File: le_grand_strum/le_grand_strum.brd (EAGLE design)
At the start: 186.9 x 99.1 mm, 101 parts, among them IC1 REG1117, IC2 PIC16F1825SO14, IC3 74HC595D, IC4 74HC595D, SW1 12MMTACT_SMT, SW10 12MMTACT_SMT, SW11 12MMTACT_SMT, SW12 12MMTACT_SMT, SW13 12MMTACT_SMT, SW14 12MMTACT_SMT, SW15 12MMTACT_SMT, SW16 12MMTACT_SMT, SW17 12MMTACT_SMT, SW18 12MMTACT_SMT, SW19 12MMTACT_SMT, SW2 12MMTACT_SMT, SW20 12MMTACT_SMT, SW21 12MMTACT_SMT, SW22 12MMTACT_SMT, SW23 12MMTACT_SMT, SW24 12MMTACT_SMT, SW25 12MMTACT_SMT, SW26 12MMTACT_SMT, SW27 12MMTACT_SMT, SW28 12MMTACT_SMT, SW29 12MMTACT_SMT, SW3 12MMTACT_SMT, SW30 12MMTACT_SMT, SW31 12MMTACT_SMT, SW32 12MMTACT_SMT, SW33 12MMTACT_SMT, SW34 12MMTACT_SMT, SW35 12MMTACT_SMT, SW36 12MMTACT_SMT, SW4 12MMTACT_SMT, SW5 12MMTACT_SMT, SW6 12MMTACT_SMT, SW7 12MMTACT_SMT, SW8 12MMTACT_SMT, SW9 12MMTACT_SMT

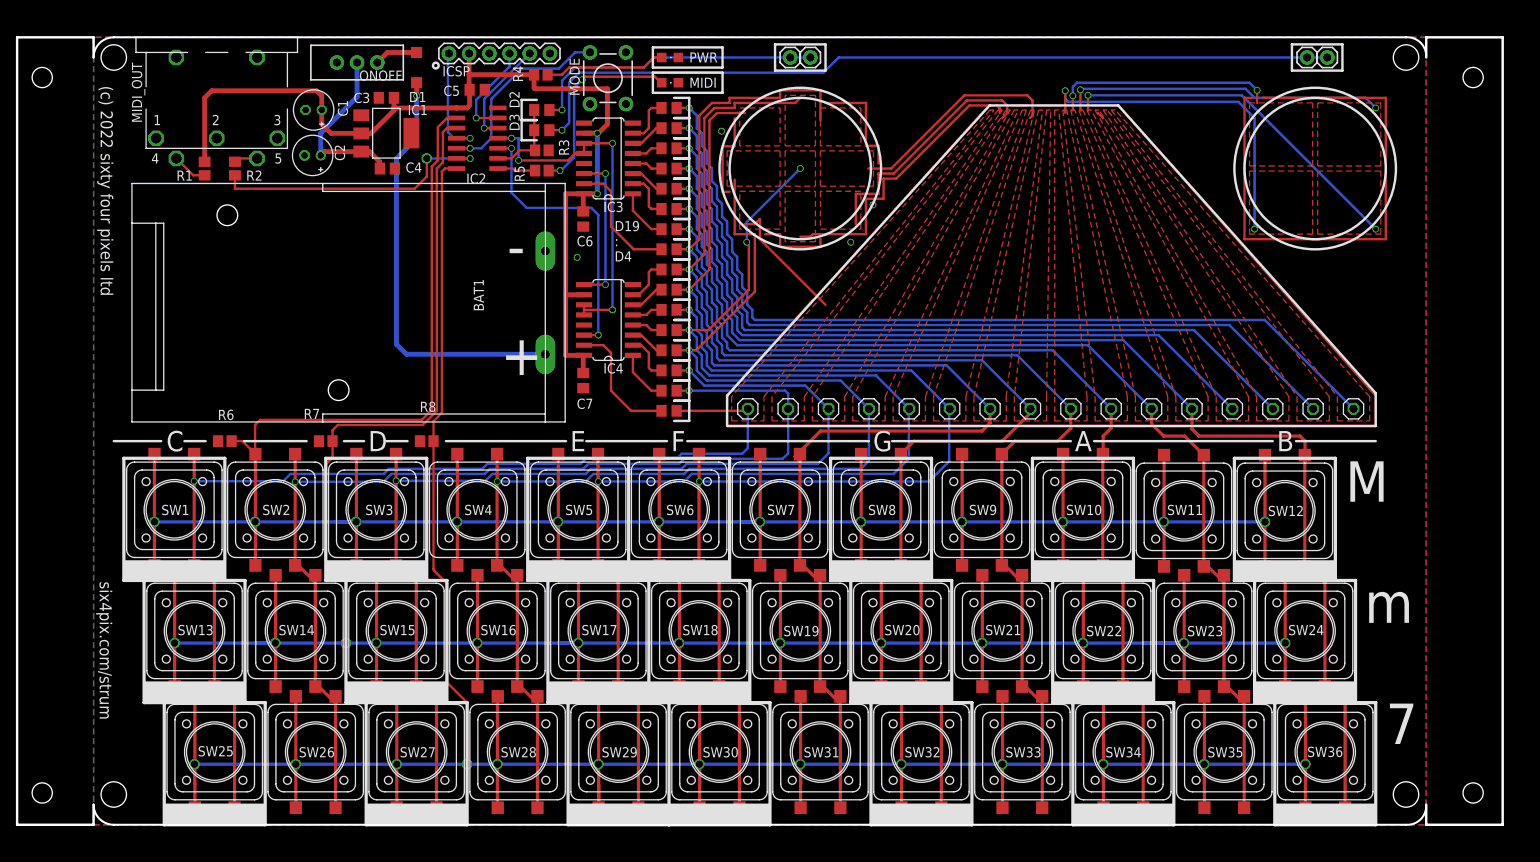
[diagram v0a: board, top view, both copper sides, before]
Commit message: rev2 board thru hole switches
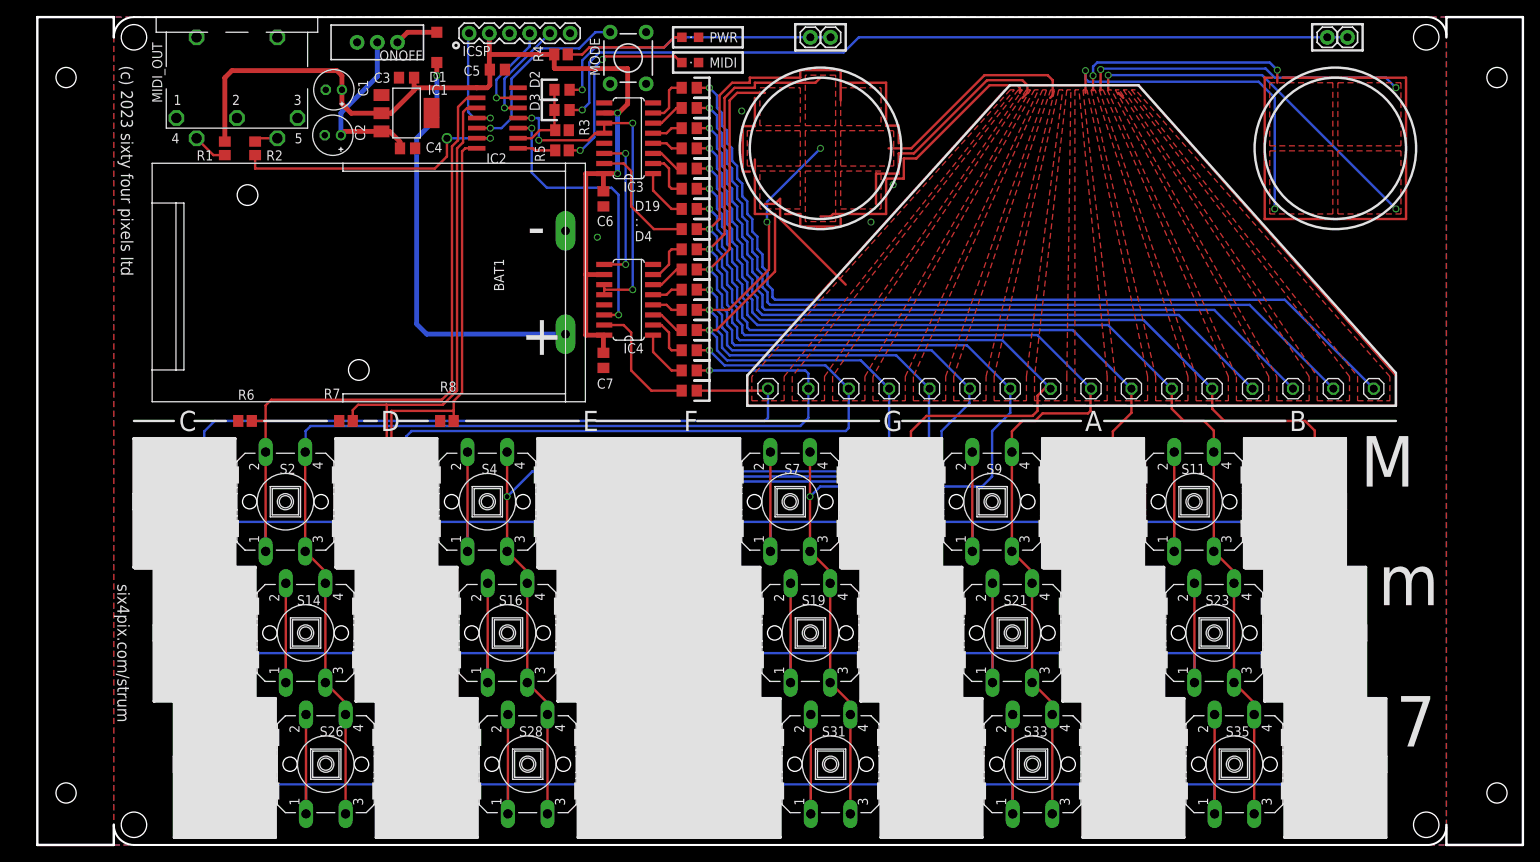
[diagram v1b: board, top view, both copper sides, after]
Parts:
- removed SW1, SW10, SW11, SW12, SW13, SW14, SW15, SW16, SW17, SW18, SW19, SW2, SW20, SW21, SW22, SW23, SW24, SW25, SW26, SW27, SW28, SW29, SW3, SW30, SW31, SW32, SW33, SW34, SW35, SW36, SW4, SW5, SW6, SW7, SW8, SW9: 12MMTACT_SMT, jason_eagle6:12MMTACT_SMT
- added S1, S10, S11, S12, S13, S14, S15, S16, S17, S18, S19, S2, S20, S21, S22, S23, S24, S25, S26, S27, S28, S29, S3, S30, S31, S32, S33, S34, S35, S36, S4, S5, S6, S7, S8, S9: (no value), switch-omron:B3F-40XX
- moved 14 3.59 mm to (148.3, 54.9)
- moved 16 3.59 mm to (158.5, 54.9)
- moved D11 3.59 mm to (72.4, 72.4)
- moved D12 3.59 mm to (72.4, 74.9)
- moved D14 3.59 mm to (72.4, 80.0)
- moved D16 3.59 mm to (72.4, 85.1)
- moved D18 3.59 mm to (72.4, 90.2)
- moved D9 3.59 mm to (72.4, 67.3)
- moved MODE 3.59 mm to (64.7, 96.5)
- moved STYLUS2 3.59 mm to (90.2, 99.1)
- moved C2 3.59 mm to (27.6, 86.7)
- moved R1 3.59 mm to (14.0, 85.1)
- moved R2 3.59 mm to (17.8, 85.1)
- moved 1 3.59 mm to (82.3, 54.9)
- moved 2 3.59 mm to (87.4, 54.9)
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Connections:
- net LINE1: now also S1.3, S1.4, S13.3, S13.4, S25.3, S25.4; no longer SW1.B1, SW1.B2, SW13.B1, SW13.B2, SW25.B1, SW25.B2
- net LINE10: now also S10.3, S10.4, S22.3, S22.4, S34.3, S34.4; no longer SW10.B1, SW10.B2, SW22.B1, SW22.B2, SW34.B1, SW34.B2
- net LINE11: now also S11.3, S11.4, S23.3, S23.4, S35.3, S35.4; no longer SW11.B1, SW11.B2, SW23.B1, SW23.B2, SW35.B1, SW35.B2
- net LINE12: now also S12.3, S12.4, S24.3, S24.4, S36.3, S36.4; no longer SW12.B1, SW12.B2, SW24.B1, SW24.B2, SW36.B1, SW36.B2
- net LINE2: now also S14.3, S14.4, S2.3, S2.4, S26.3, S26.4; no longer SW14.B1, SW14.B2, SW2.B1, SW2.B2, SW26.B1, SW26.B2
- net LINE3: now also S15.3, S15.4, S27.3, S27.4, S3.3, S3.4; no longer SW15.B1, SW15.B2, SW27.B1, SW27.B2, SW3.B1, SW3.B2
- net LINE4: now also S16.3, S16.4, S28.3, S28.4, S4.3, S4.4; no longer SW16.B1, SW16.B2, SW28.B1, SW28.B2, SW4.B1, SW4.B2
- net LINE5: now also S17.3, S17.4, S29.3, S29.4, S5.3, S5.4; no longer SW17.B1, SW17.B2, SW29.B1, SW29.B2, SW5.B1, SW5.B2
- net LINE6: now also S18.3, S18.4, S30.3, S30.4, S6.3, S6.4; no longer SW18.B1, SW18.B2, SW30.B1, SW30.B2, SW6.B1, SW6.B2
- net LINE7: now also S19.3, S19.4, S31.3, S31.4, S7.3, S7.4; no longer SW19.B1, SW19.B2, SW31.B1, SW31.B2, SW7.B1, SW7.B2
- net LINE8: now also S20.3, S20.4, S32.3, S32.4, S8.3, S8.4; no longer SW20.B1, SW20.B2, SW32.B1, SW32.B2, SW8.B1, SW8.B2
- net LINE9: now also S21.3, S21.4, S33.3, S33.4, S9.3, S9.4; no longer SW21.B1, SW21.B2, SW33.B1, SW33.B2, SW9.B1, SW9.B2
- net RA4: now also S13.1, S13.2, S14.1, S14.2, S15.1, S15.2, S16.1, S16.2, S17.1, S17.2, S18.1, S18.2, S19.1, S19.2, S20.1, S20.2, S21.1, S21.2, S22.1, S22.2, S23.1, S23.2, S24.1, S24.2; no longer SW13.A1, SW13.A2, SW14.A1, SW14.A2, SW15.A1, SW15.A2, SW16.A1, SW16.A2, SW17.A1, SW17.A2, SW18.A1, SW18.A2, SW19.A1, SW19.A2, SW20.A1, SW20.A2, SW21.A1, SW21.A2, SW22.A1, SW22.A2, SW23.A1, SW23.A2, SW24.A1, SW24.A2
- net RA5: now also S1.1, S1.2, S10.1, S10.2, S11.1, S11.2, S12.1, S12.2, S2.1, S2.2, S3.1, S3.2, S4.1, S4.2, S5.1, S5.2, S6.1, S6.2, S7.1, S7.2, S8.1, S8.2, S9.1, S9.2; no longer SW1.A1, SW1.A2, SW10.A1, SW10.A2, SW11.A1, SW11.A2, SW12.A1, SW12.A2, SW2.A1, SW2.A2, SW3.A1, SW3.A2, SW4.A1, SW4.A2, SW5.A1, SW5.A2, SW6.A1, SW6.A2, SW7.A1, SW7.A2, SW8.A1, SW8.A2, SW9.A1, SW9.A2
- net RC3: now also S25.1, S25.2, S26.1, S26.2, S27.1, S27.2, S28.1, S28.2, S29.1, S29.2, S30.1, S30.2, S31.1, S31.2, S32.1, S32.2, S33.1, S33.2, S34.1, S34.2, S35.1, S35.2, S36.1, S36.2; no longer SW25.A1, SW25.A2, SW26.A1, SW26.A2, SW27.A1, SW27.A2, SW28.A1, SW28.A2, SW29.A1, SW29.A2, SW30.A1, SW30.A2, SW31.A1, SW31.A2, SW32.A1, SW32.A2, SW33.A1, SW33.A2, SW34.A1, SW34.A2, SW35.A1, SW35.A2, SW36.A1, SW36.A2
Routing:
- net RA5: track 383.5 -> 403.5 mm, vias 12 -> 0
- net RC3: track 406.5 -> 416.1 mm, vias 13 -> 0
- net RA4: track 399.4 -> 408.2 mm, vias 13 -> 0
- net LINE7: track 154.3 -> 160.1 mm, vias 1 -> 2
- net N$28: track 33.0 -> 37.1 mm
- net LINE8: track 157.4 -> 161.0 mm
- net N$29: track 1.91 -> 0.00 mm
- net LINE12: track 193.3 -> 191.5 mm
- net LINE9: track 164.0 -> 165.8 mm
- net LINE6: track 160.8 -> 159.8 mm
- net N$33: track 3.18 -> 3.81 mm
- net LINE5: track 161.9 -> 162.5 mm
- net LINE1: track 151.5 -> 151.0 mm, vias 1 -> 0
- net LINE4: track 162.8 -> 163.3 mm
- net LINE3: track 162.7 -> 163.1 mm, vias 2 -> 1
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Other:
- board size 186.9 x 99.1 mm -> 186.9 x 104.1 mm
- board text added: "(c) 2023 sixty four pixels ltd"
- board text added: "LE GRAND STRUM REV2 hotchk155/2023"
- board text removed: "(c) 2022 sixty four pixels ltd"
- board text removed: "LE GRAND STRUM PCB REV1 hotchk155/2022"
